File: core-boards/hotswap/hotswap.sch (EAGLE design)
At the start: 15 parts, among them J1 WALL, J2 BATTERY, J3 COMPUTER, Q1 SUP75P03_07, Q2 SUP75P03_07, Q3 SUP75P03_07, U1 LTC4416EMS#PBF

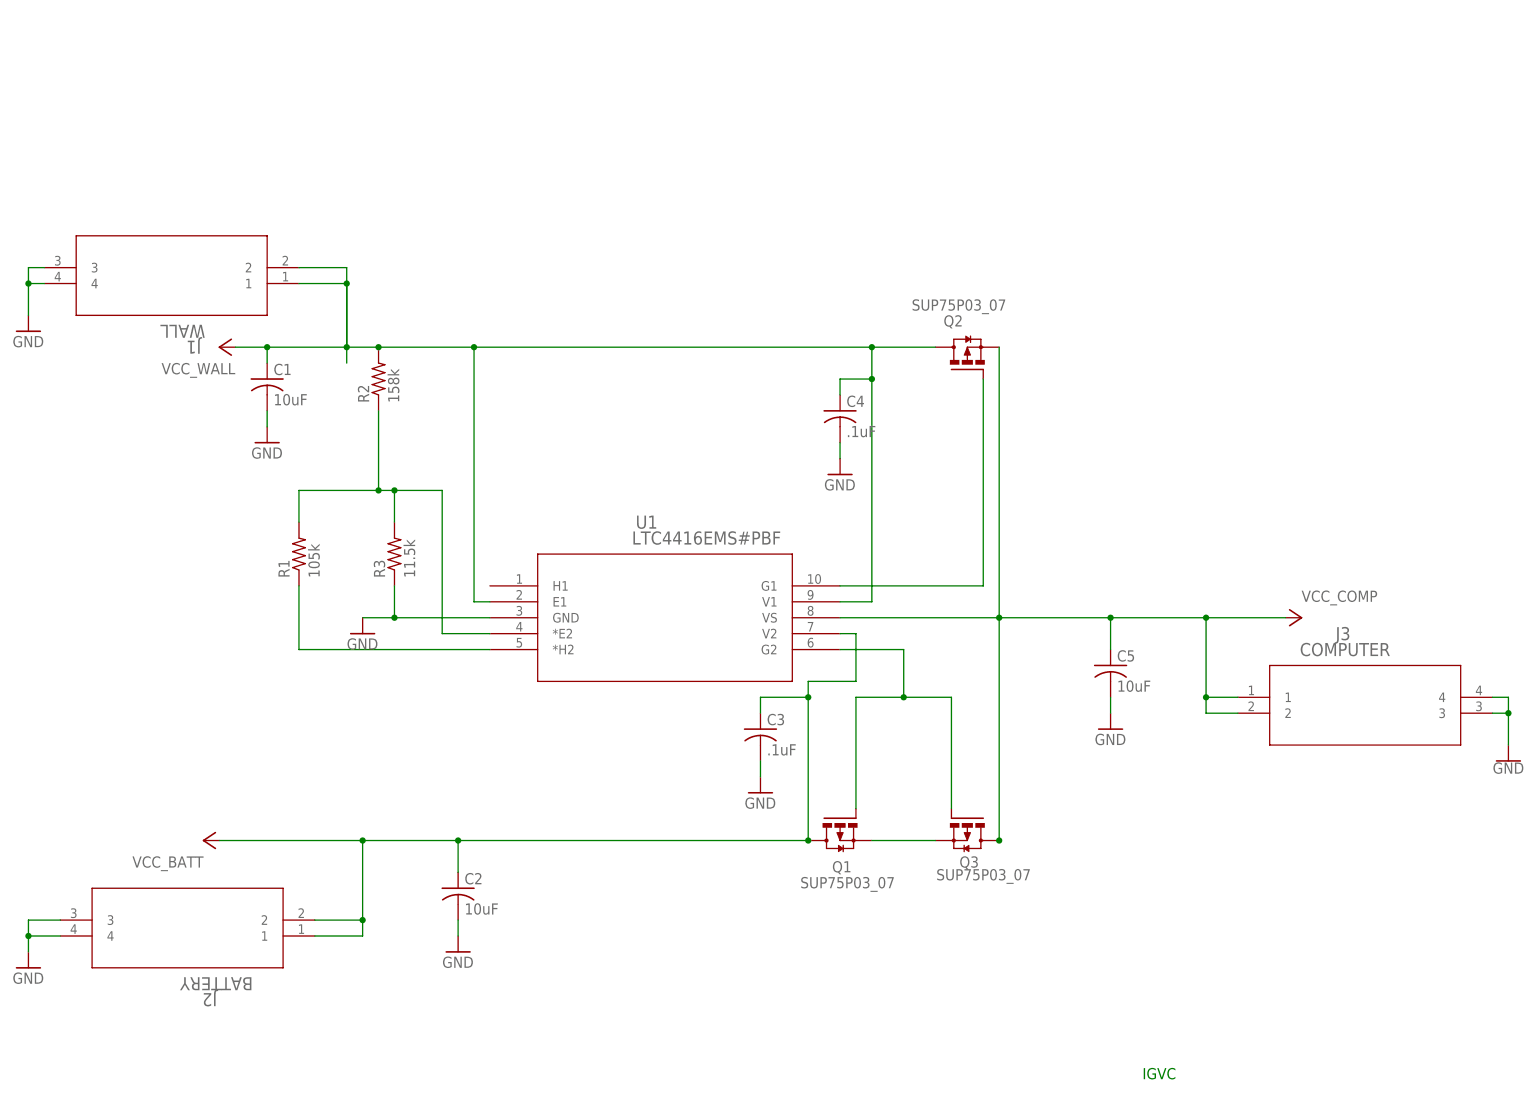
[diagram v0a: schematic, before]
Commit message: Added new connector
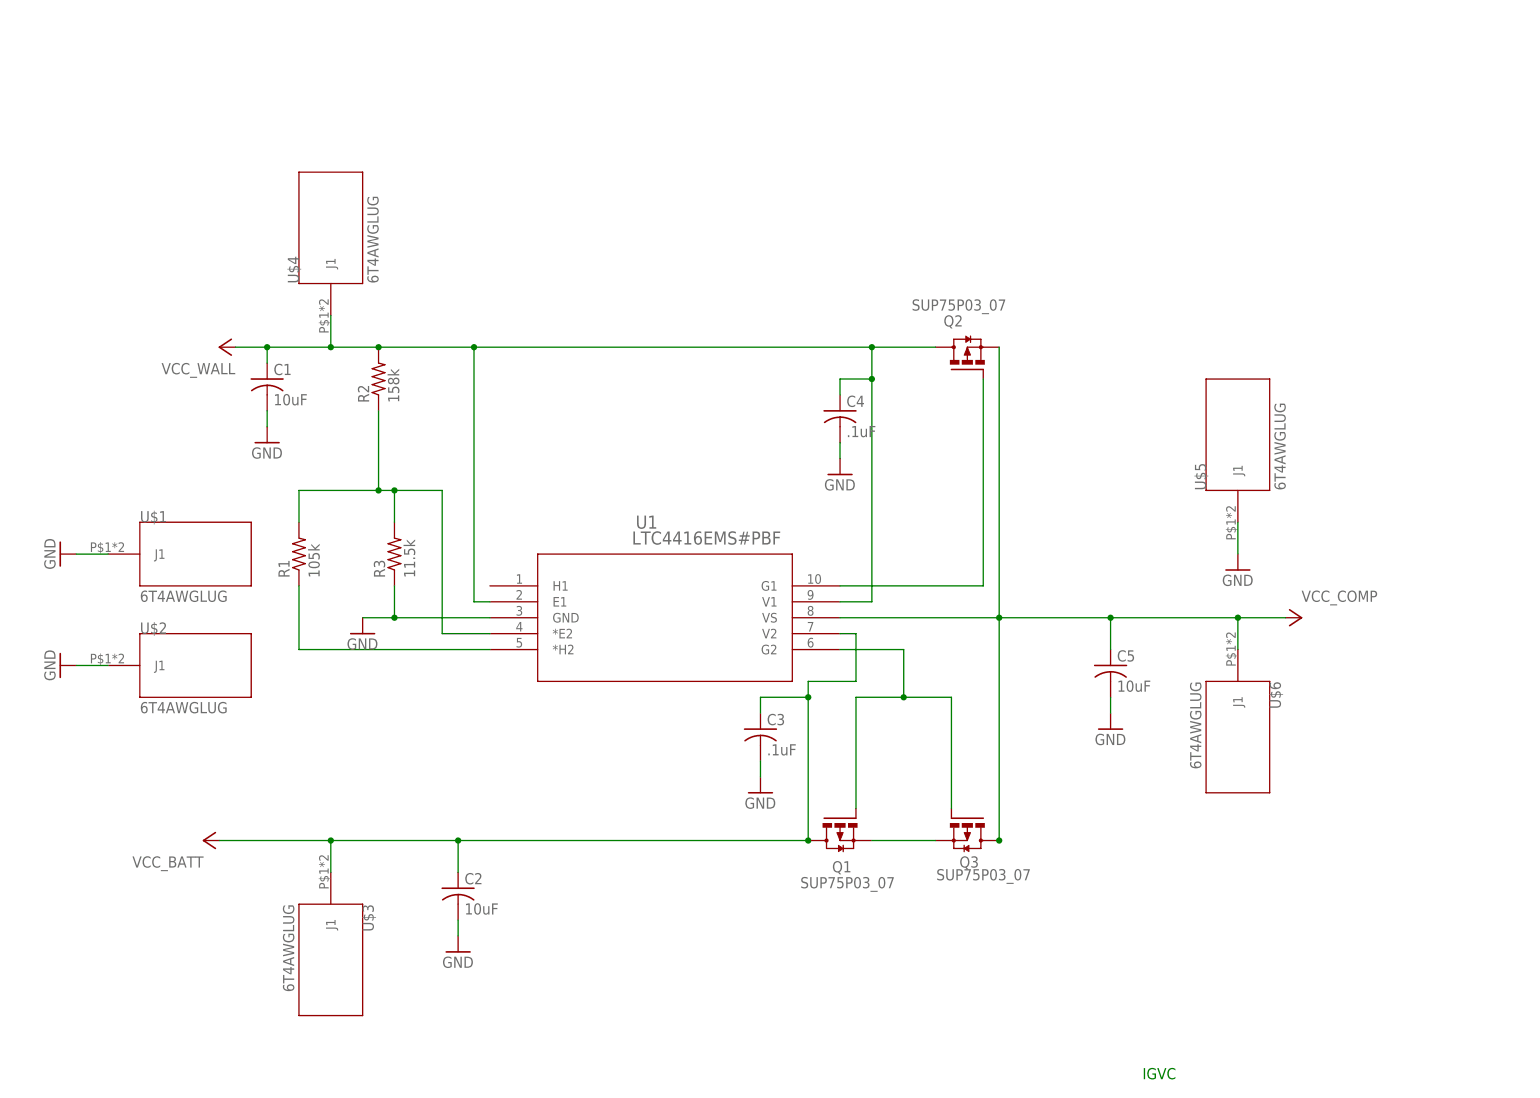
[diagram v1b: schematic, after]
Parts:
- removed J1: WALL, IGVC-Connector:641737-1
- removed J2: BATTERY, IGVC-Connector:641737-1
- removed J3: COMPUTER, IGVC-Connector:641737-1
- added U$1, U$2, U$3, U$4, U$5, U$6: 6T4AWGLUG, IGVC-Connector:6T4AWGLUG
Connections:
- net GND: now also U$1.J1, U$2.J1, U$5.J1; no longer J1.3, J1.4, J2.3, J2.4, J3.3, J3.4
- net VCC_BATT: now also U$3.J1; no longer J2.1, J2.2
- net VCC_COMP: now also U$6.J1; no longer J3.1, J3.2
- net VCC_WALL: now also U$4.J1; no longer J1.1, J1.2

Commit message: Routed the Board
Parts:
- removed U$3, U$4: 6T4AWGLUG, IGVC-Connector:6T4AWGLUG
- added VCC_BATT, VCC_WALL: 6T4AWGLUG, IGVC-Connector:6T4AWGLUG
- renumbered U$5 to VCC_COMP
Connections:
- net VCC_BATT: now also VCC_BATT.J1; no longer U$3.J1
- net VCC_WALL: now also VCC_WALL.J1; no longer U$4.J1
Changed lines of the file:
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@@
 <part name="U$1" library="IGVC-Connector" deviceset="6T4AWGLUG" device=""/>
 <part name="U$2" library="IGVC-Connector" deviceset="6T4AWGLUG" device=""/>
-<part name="U$3" library="IGVC-Connector" deviceset="6T4AWGLUG" device=""/>
-<part name="U$4" library="IGVC-Connector" deviceset="6T4AWGLUG" device=""/>
-<part name="U$5" library="IGVC-Connector" deviceset="6T4AWGLUG" device=""/>
+<part name="VCC_BATT" library="IGVC-Connector" deviceset="6T4AWGLUG" device=""/>
+<part name="VCC_WALL" library="IGVC-Connector" deviceset="6T4AWGLUG" device=""/>
+<part name="VCC_COMP" library="IGVC-Connector" deviceset="6T4AWGLUG" device=""/>
 <part name="U$6" library="IGVC-Connector" deviceset="6T4AWGLUG" device=""/>
 </parts>
@@
 <attribute name="VALUE" x="-17.78" y="17.78" size="1.778" layer="96"/>
 </instance>
-<instance part="U$3" gate="6T4AWGLUG" x="12.7" y="-17.78" smashed="yes" rot="R270">
-<attribute name="NAME" x="17.78" y="-12.7" size="1.778" layer="95" rot="R270"/>
-<attribute name="VALUE" x="5.08" y="-12.7" size="1.778" layer="96" rot="R270"/>
-</instance>
-<instance part="U$4" gate="6T4AWGLUG" x="12.7" y="91.44" smashed="yes" rot="R90">
-<attribute name="NAME" x="7.62" y="86.36" size="1.778" layer="95" rot="R90"/>
-<attribute name="VALUE" x="20.32" y="86.36" size="1.778" layer="96" rot="R90"/>
-</instance>
-<instance part="U$5" gate="6T4AWGLUG" x="157.48" y="58.42" smashed="yes" rot="R90">
+<instance part="VCC_BATT" gate="6T4AWGLUG" x="7.62" y="-17.78" smashed="yes" rot="R270">
+<attribute name="NAME" x="12.7" y="-12.7" size="1.778" layer="95" rot="R270"/>
+<attribute name="VALUE" x="0" y="-12.7" size="1.778" layer="96" rot="R270"/>
+</instance>
+<instance part="VCC_WALL" gate="6T4AWGLUG" x="7.62" y="91.44" smashed="yes" rot="R90">
+<attribute name="NAME" x="2.54" y="86.36" size="1.778" layer="95" rot="R90"/>
+<attribute name="VALUE" x="15.24" y="86.36" size="1.778" layer="96" rot="R90"/>
+</instance>
+<instance part="VCC_COMP" gate="6T4AWGLUG" x="157.48" y="58.42" smashed="yes" rot="R90">
 <attribute name="NAME" x="152.4" y="53.34" size="1.778" layer="95" rot="R90"/>
 <attribute name="VALUE" x="165.1" y="53.34" size="1.778" layer="96" rot="R90"/>
@@
 <pinref part="GND9" gate="1" pin="GND"/>
 <wire x1="157.48" y1="43.18" x2="157.48" y2="48.26" width="0.1524" layer="91"/>
-<pinref part="U$5" gate="6T4AWGLUG" pin="J1"/>
+<pinref part="VCC_COMP" gate="6T4AWGLUG" pin="J1"/>
 </segment>
 </net>
@@
 <pinref part="R2" gate="G$1" pin="2"/>
 <junction x="20.32" y="76.2"/>
-<wire x1="20.32" y1="76.2" x2="12.7" y2="76.2" width="0.1524" layer="91"/>
-<wire x1="12.7" y1="76.2" x2="2.54" y2="76.2" width="0.1524" layer="91"/>
+<wire x1="20.32" y1="76.2" x2="7.62" y2="76.2" width="0.1524" layer="91"/>
+<wire x1="7.62" y1="76.2" x2="2.54" y2="76.2" width="0.1524" layer="91"/>
 <wire x1="2.54" y1="76.2" x2="-2.54" y2="76.2" width="0.1524" layer="91"/>
 <wire x1="2.54" y1="76.2" x2="2.54" y2="73.66" width="0.1524" layer="91"/>
@@
 <wire x1="109.22" y1="76.2" x2="99.06" y2="76.2" width="0.1524" layer="91"/>
 <junction x="99.06" y="76.2"/>
-<wire x1="12.7" y1="81.28" x2="12.7" y2="76.2" width="0.1524" layer="91"/>
-<junction x="12.7" y="76.2"/>
-<pinref part="U$4" gate="6T4AWGLUG" pin="J1"/>
+<wire x1="7.62" y1="81.28" x2="7.62" y2="76.2" width="0.1524" layer="91"/>
+<junction x="7.62" y="76.2"/>
+<pinref part="VCC_WALL" gate="6T4AWGLUG" pin="J1"/>
 </segment>
 </net>
@@
 <wire x1="88.9" y1="-2.54" x2="33.02" y2="-2.54" width="0.1524" layer="91"/>
 <pinref part="P+1" gate="VCC" pin="VCC"/>
-<wire x1="33.02" y1="-2.54" x2="12.7" y2="-2.54" width="0.1524" layer="91"/>
-<wire x1="12.7" y1="-2.54" x2="-5.08" y2="-2.54" width="0.1524" layer="91"/>
+<wire x1="33.02" y1="-2.54" x2="7.62" y2="-2.54" width="0.1524" layer="91"/>
+<wire x1="7.62" y1="-2.54" x2="-5.08" y2="-2.54" width="0.1524" layer="91"/>
 <wire x1="33.02" y1="-2.54" x2="33.02" y2="-7.62" width="0.1524" layer="91"/>
 <junction x="33.02" y="-2.54"/>
@@
 <junction x="88.9" y="20.32"/>
 <pinref part="C3" gate="G$1" pin="1"/>
-<wire x1="12.7" y1="-7.62" x2="12.7" y2="-2.54" width="0.1524" layer="91"/>
-<junction x="12.7" y="-2.54"/>
-<pinref part="U$3" gate="6T4AWGLUG" pin="J1"/>
-</segment>
-</net>
+<wire x1="7.62" y1="-7.62" x2="7.62" y2="-2.54" width="0.1524" layer="91"/>
+<junction x="7.62" y="-2.54"/>
+<pinref part="VCC_BATT" gate="6T4AWGLUG" pin="J1"/>
+</segment>
+</net>

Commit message: Finish Optisolators
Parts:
- added J1: 2-PIN_2MM-V, RoboJackets-Connectors:2-PIN_2MM-V
- added Z1: TLP2745, IGVC-Discrete:TLP2745
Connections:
- new net N$2: J1.1, Z1.P$5
- new net VCC: Z1.P$4
- net GND: now also Z1.P$3, Z1.P$6
- net VCC_WALL: now also Z1.P$1
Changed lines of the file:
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@@
 <layer number="115" name="ReferenceISLANDS" color="7" fill="1" visible="no" active="yes"/>
 <layer number="116" name="Patch_BOT" color="9" fill="4" visible="yes" active="yes"/>
+<layer number="117" name="BACKMAAT1" color="7" fill="1" visible="yes" active="yes"/>
 <layer number="118" name="Rect_Pads" color="7" fill="1" visible="no" active="yes"/>
+<layer number="119" name="KAP_TEKEN" color="7" fill="1" visible="yes" active="yes"/>
+<layer number="120" name="KAP_MAAT1" color="7" fill="1" visible="yes" active="yes"/>
 <layer number="121" name="_tsilk" color="7" fill="1" visible="yes" active="yes"/>
 <layer number="122" name="_bsilk" color="7" fill="1" visible="yes" active="yes"/>
@@
 <layer number="128" name="_bValues" color="7" fill="1" visible="yes" active="yes"/>
 <layer number="129" name="Mask" color="7" fill="1" visible="yes" active="yes"/>
+<layer number="130" name="SMDSTROOK" color="7" fill="1" visible="yes" active="yes"/>
 <layer number="131" name="tAdjust" color="7" fill="1" visible="yes" active="yes"/>
 <layer number="132" name="bAdjust" color="7" fill="1" visible="yes" active="yes"/>
@@
 <layer number="230" name="230bmp" color="7" fill="1" visible="yes" active="yes"/>
 <layer number="231" name="231bmp" color="7" fill="1" visible="yes" active="yes"/>
+<layer number="232" name="Eagle3D_PG2" color="7" fill="1" visible="yes" active="yes"/>
+<layer number="233" name="Eagle3D_PG3" color="7" fill="1" visible="yes" active="yes"/>
 <layer number="248" name="Housing" color="7" fill="1" visible="yes" active="yes"/>
 <layer number="249" name="Edge" color="7" fill="1" visible="yes" active="yes"/>
@@
 <part name="VCC_COMP" library="IGVC-Connector" deviceset="6T4AWGLUG" device=""/>
 <part name="U$6" library="IGVC-Connector" deviceset="6T4AWGLUG" device=""/>
+<part name="Z1" library="IGVC-Discrete" deviceset="TLP2745" device=""/>
+<part name="P+4" library="supply1" library_urn="urn:adsk.eagle:library:371" deviceset="VCC" device=""/>
+<part name="GND10" library="supply1" library_urn="urn:adsk.eagle:library:371" deviceset="GND" device=""/>
+<part name="GND11" library="supply1" library_urn="urn:adsk.eagle:library:371" deviceset="GND" device=""/>
+<part name="J1" library="RoboJackets-Connectors" deviceset="2-PIN_2MM-*" device="V"/>
 </parts>
 <sheets>
@@
 <attribute name="VALUE" x="149.86" y="22.86" size="1.778" layer="96" rot="R270"/>
 </instance>
+<instance part="Z1" gate="TLP2745" x="66.04" y="96.52" smashed="yes">
+<attribute name="NAME" x="55.88" y="104.14" size="1.778" layer="125"/>
+<attribute name="VALUE" x="55.88" y="86.36" size="1.778" layer="127"/>
+</instance>
+<instance part="P+4" gate="VCC" x="88.9" y="101.6" smashed="yes" rot="R270">
+<attribute name="VALUE" x="86.36" y="104.14" size="1.778" layer="96"/>
+</instance>
+<instance part="GND10" gate="1" x="88.9" y="91.44" smashed="yes" rot="R90">
+<attribute name="VALUE" x="91.44" y="88.9" size="1.778" layer="96" rot="R90"/>
+</instance>
+<instance part="GND11" gate="1" x="43.18" y="101.6" smashed="yes" rot="R270">
+<attribute name="VALUE" x="40.64" y="104.14" size="1.778" layer="96" rot="R270"/>
+</instance>
+<instance part="J1" gate="G$1" x="119.38" y="99.06" smashed="yes" rot="R180">
+<attribute name="NAME" x="124.46" y="91.44" size="1.778" layer="95" font="vector" rot="R180" align="top-left"/>
+<attribute name="VALUE" x="124.46" y="106.68" size="1.778" layer="96" font="vector" rot="R180"/>
+</instance>
 </instances>
 <busses>
@@
 <pinref part="VCC_COMP" gate="6T4AWGLUG" pin="J1"/>
 </segment>
+<segment>
+<pinref part="Z1" gate="TLP2745" pin="P$6"/>
+<pinref part="GND10" gate="1" pin="GND"/>
+<wire x1="81.28" y1="91.44" x2="86.36" y2="91.44" width="0.1524" layer="91"/>
+</segment>
+<segment>
+<pinref part="GND11" gate="1" pin="GND"/>
+<pinref part="Z1" gate="TLP2745" pin="P$3"/>
+<wire x1="45.72" y1="101.6" x2="50.8" y2="101.6" width="0.1524" layer="91"/>
+</segment>
 </net>
 <net name="N$4" class="0">
@@
 <pinref part="P+2" gate="VCC" pin="VCC"/>
 <wire x1="20.32" y1="76.2" x2="35.56" y2="76.2" width="0.1524" layer="91"/>
-<wire x1="35.56" y1="76.2" x2="99.06" y2="76.2" width="0.1524" layer="91"/>
+<wire x1="35.56" y1="76.2" x2="38.1" y2="76.2" width="0.1524" layer="91"/>
+<wire x1="38.1" y1="76.2" x2="99.06" y2="76.2" width="0.1524" layer="91"/>
 <wire x1="99.06" y1="76.2" x2="99.06" y2="71.12" width="0.1524" layer="91"/>
 <pinref part="U1" gate="A" pin="V1"/>
@@
 <junction x="7.62" y="76.2"/>
 <pinref part="VCC_WALL" gate="6T4AWGLUG" pin="J1"/>
+<pinref part="Z1" gate="TLP2745" pin="P$1"/>
+<wire x1="38.1" y1="76.2" x2="38.1" y2="96.52" width="0.1524" layer="91"/>
+<wire x1="38.1" y1="96.52" x2="50.8" y2="96.52" width="0.1524" layer="91"/>
+<junction x="38.1" y="76.2"/>
 </segment>
 </net>
@@
 </segment>
 </net>
+<net name="VCC" class="0">
+<segment>
+<pinref part="Z1" gate="TLP2745" pin="P$4"/>
+<pinref part="P+4" gate="VCC" pin="VCC"/>
+<wire x1="81.28" y1="101.6" x2="86.36" y2="101.6" width="0.1524" layer="91"/>
+</segment>
+</net>
+<net name="N$2" class="0">
+<segment>
+<pinref part="Z1" gate="TLP2745" pin="P$5"/>
+<pinref part="J1" gate="G$1" pin="1"/>
+<wire x1="81.28" y1="96.52" x2="114.3" y2="96.52" width="0.1524" layer="91"/>
+</segment>
+</net>

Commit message: Finishing touches to the board
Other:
- moved on the sheet: C1, C2, C3, C4, C5, J1, Q1, Q2, Q3, R1, R2, R3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

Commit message: Minor tweaks
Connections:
- net VCC_COMP renamed VCC_ROBOT
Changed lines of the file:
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@@
 <attribute name="VALUE" x="10.16" y="91.44" size="1.778" layer="96" rot="R180"/>
 </instance>
-<instance part="P+3" gate="VCC" x="180.34" y="50.8" smashed="yes" rot="R270">
-<attribute name="VALUE" x="180.34" y="53.34" size="1.778" layer="96"/>
-</instance>
+<instance part="P+3" gate="VCC" x="180.34" y="50.8" smashed="yes" rot="R270"/>
 <instance part="FRAME1" gate="G$1" x="-48.26" y="-71.12" smashed="yes"/>
 <instance part="FRAME1" gate="G$2" x="124.46" y="-71.12" smashed="yes">
@@
 </segment>
 </net>
-<net name="VCC_COMP" class="0">
+<net name="VCC_ROBOT" class="0">
 <segment>
 <pinref part="U1" gate="A" pin="VS"/>
@@
 <junction x="170.18" y="50.8"/>
 <pinref part="U$6" gate="6T4AWGLUG" pin="J1"/>
-</segment>
-</net>
+<label x="182.88" y="50.8" size="1.778" layer="95"/>
+</segment>
+</net>

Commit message: Hotswap 2/9/2020
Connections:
- net GND: now also J1.2
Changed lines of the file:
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@@
 <part name="GND11" library="supply1" library_urn="urn:adsk.eagle:library:371" deviceset="GND" device=""/>
 <part name="J1" library="RoboJackets-Connectors" deviceset="2-PIN_2MM-*" device="V"/>
+<part name="GND12" library="supply1" library_urn="urn:adsk.eagle:library:371" deviceset="GND" device=""/>
 </parts>
 <sheets>
@@
 <attribute name="VALUE" x="137.16" y="124.46" size="1.778" layer="96" font="vector" rot="R180"/>
 </instance>
+<instance part="GND12" gate="1" x="119.38" y="119.38" smashed="yes" rot="R270">
+<attribute name="VALUE" x="116.84" y="121.92" size="1.778" layer="96" rot="R270"/>
+</instance>
 </instances>
 <busses>
@@
 <wire x1="58.42" y1="119.38" x2="63.5" y2="119.38" width="0.1524" layer="91"/>
 </segment>
+<segment>
+<pinref part="GND12" gate="1" pin="GND"/>
+<pinref part="J1" gate="G$1" pin="2"/>
+<wire x1="121.92" y1="119.38" x2="127" y2="119.38" width="0.1524" layer="91"/>
+</segment>
 </net>
